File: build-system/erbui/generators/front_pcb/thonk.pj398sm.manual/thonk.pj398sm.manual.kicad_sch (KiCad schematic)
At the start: 1 part, among them J1 IN

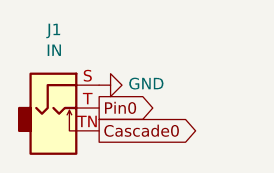
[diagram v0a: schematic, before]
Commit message: Replace cascade feature with normalling feature
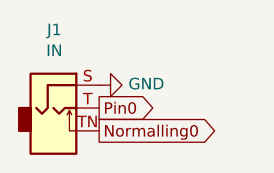
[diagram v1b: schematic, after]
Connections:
- net Cascade0 renamed Normalling0
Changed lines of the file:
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@@
 (kicad_sch (version 20211123) (generator eeschema)
   (paper "A4")
-  (global_label "Cascade0" (shape output) (at 97.79 109.22 0) (fields_autoplaced)
+  (global_label "Normalling0" (shape output) (at 97.79 109.22 0) (fields_autoplaced)
     (effects (font (size 1.27 1.27)) (justify left))
-    (property "Intersheet References" "${INTERSHEET_REFS}" (id 0) (at 0 0 0)
-      (effects (font (size 1.27 1.27)) hide)
+    (property "Intersheet References" "${INTERSHEET_REFS}" (id 0) (at 111.6652 109.1406 0)
+      (effects (font (size 1.27 1.27)) (justify left) hide)
     )
   )
